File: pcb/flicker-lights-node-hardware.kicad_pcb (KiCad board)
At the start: 2 copper layers, 59.7 x 48.9 mm, 31 parts, among them IC1 ATMEGA168PA-A, P1 CONN_01X06, P2 CONN_01X02, P3 CONN_02X04, P4 CONN_02X03, P5 CONN_01X04, P6 CONN_01X04, Q1 BSS138, Q2 BSS138, Q3 BSS138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

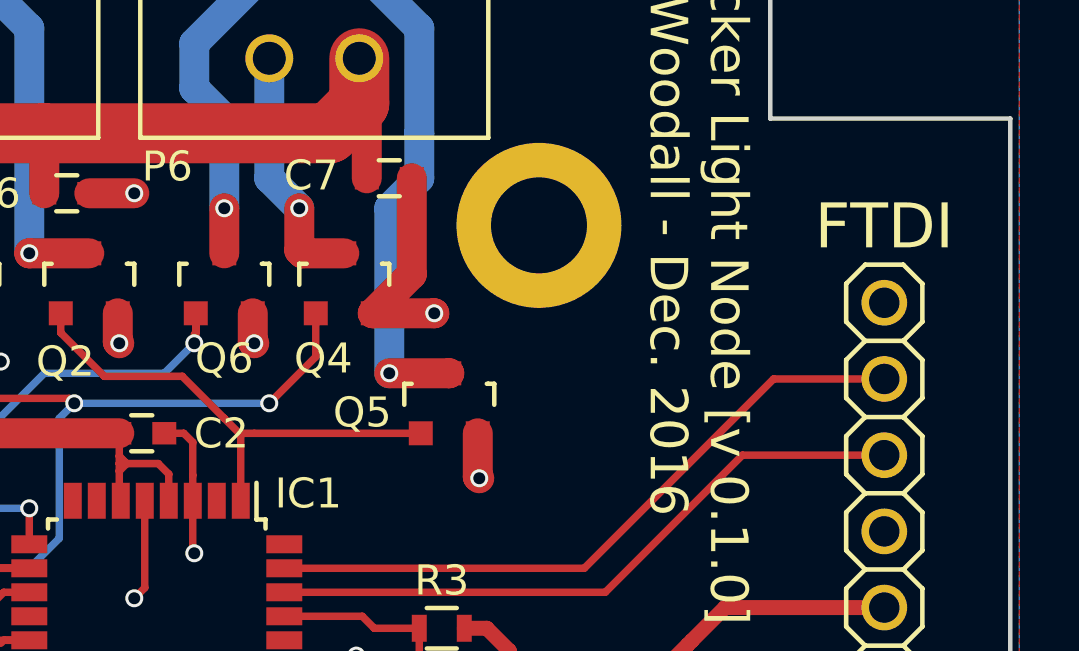
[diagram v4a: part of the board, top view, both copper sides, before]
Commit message: Made IC1 pin 1 more obvious on the PCB silkscreen
Fixes #1
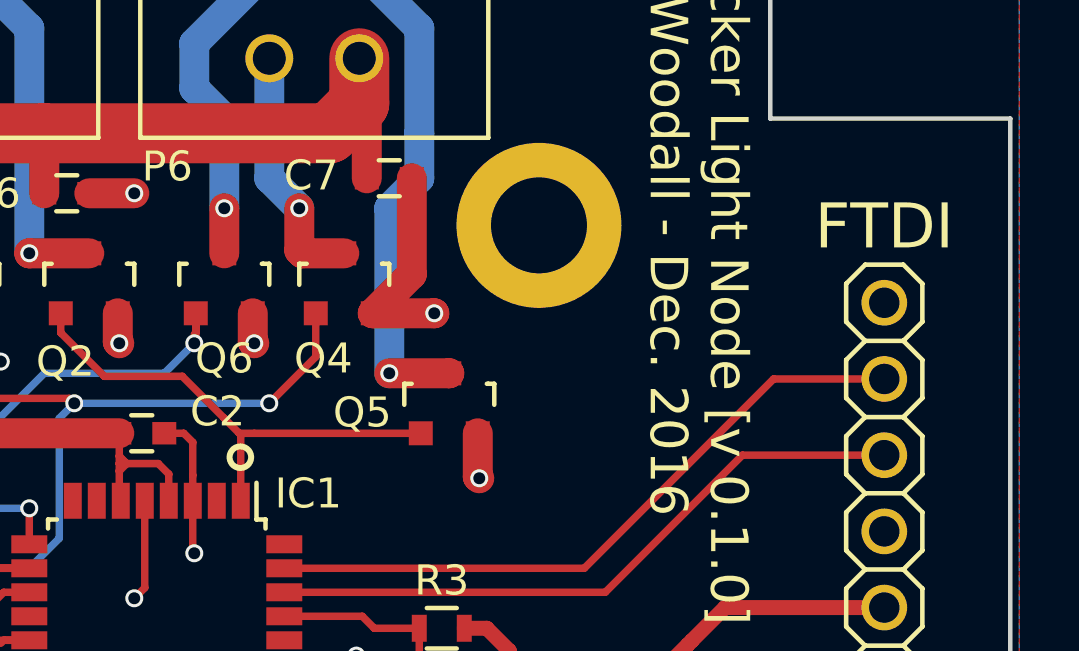
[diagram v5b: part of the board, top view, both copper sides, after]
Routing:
- net GND: vias 18 -> 17
- net (no net): vias 0 -> 1
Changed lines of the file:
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@@
 (kicad_pcb (version 4) (host pcbnew 4.0.4-1.fc25-product)
   (general
-    (links 0)
-    (no_connects 3)
-    (area 32.924999 158.674999 92.775001 207.715001)
+    (links 69)
+    (no_connects 1)
+    (area 17.464287 153.05 94.635715 218.800001)
     (thickness 1.6)
-    (drawings 49)
+    (drawings 50)
     (tracks 380)
     (zones 0)
@@
     (tags "capacitor 0603")
     (attr smd)
-    (fp_text reference C2 (at 2.65 0.01) (layer F.SilkS)
+    (fp_text reference C2 (at 2.524 -0.726) (layer F.SilkS)
       (effects (font (size 1 1) (thickness 0.15)))
     )
@@
       (xy -2.196552 -0.077837) (xy -2.20472 -0.070011) (xy -2.20472 0.220923) (xy -2.20472 0.220923)) (layer F.SilkS) (width 0.15))
   )
+  (gr_circle (center 67.036 177.038) (end 67.29 177.292) (layer F.SilkS) (width 0.2))
   (gr_text + (at 35.1 168.15) (layer F.SilkS)
     (effects (font (size 1.5 1.5) (thickness 0.3)))
@@
   (gr_line (start 65 203.85) (end 43.7 203.85) (layer F.SilkS) (width 0.2))
   (gr_line (start 72.5 203.85) (end 65 203.85) (layer F.SilkS) (width 0.2))
-  (gr_text FTDI (at 88.5 169.35 360) (layer F.SilkS)
+  (gr_text FTDI (at 88.5 169.35) (layer F.SilkS)
     (effects (font (size 1.5 1.5) (thickness 0.3)))
   )
@@
   )
   (gr_line (start 33 158.75) (end 92.73 158.75) (angle 90) (layer Dwgs.User) (width 0.2))
+  (via (at 59.05 173.85) (size 0.6) (drill 0.4) (layers F.Cu B.Cu) (net 0))
   (segment (start 55.5 188.214) (end 55.5 189.632) (width 1) (layer F.Cu) (net 1))
   (segment (start 55.5 189.632) (end 59.924 194.056) (width 1) (layer F.Cu) (net 1))
@@
   (segment (start 55.95 177.69) (end 56 177.74) (width 1) (layer F.Cu) (net 2))
   (via (at 56 177.74) (size 0.6) (drill 0.4) (layers F.Cu B.Cu) (net 2))
-  (via (at 59.05 173.85) (size 0.6) (drill 0.4) (layers F.Cu B.Cu) (net 2))
   (segment (start 62.95 172.24076) (end 62.95 173.19) (width 1) (layer F.Cu) (net 2))
   (segment (start 62.95 173.19) (end 63 173.24) (width 1) (layer F.Cu) (net 2))
